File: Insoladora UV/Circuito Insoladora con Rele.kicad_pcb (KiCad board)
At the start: 2 copper layers, 120 x 60 mm, 38 parts, among them J1 Entrada 5V/2A, J2 RELE1, J3 RELE2, K1 SANYOU_SRD_Form_C, K2 SANYOU_SRD_Form_C, Q1 BC548, Q2 BC548, SW1 RESET, SW2 UP, SW3 DOWN, SW4 START/STOP, U1 PIC16F886-IP, U2 PC817, U3 PC817

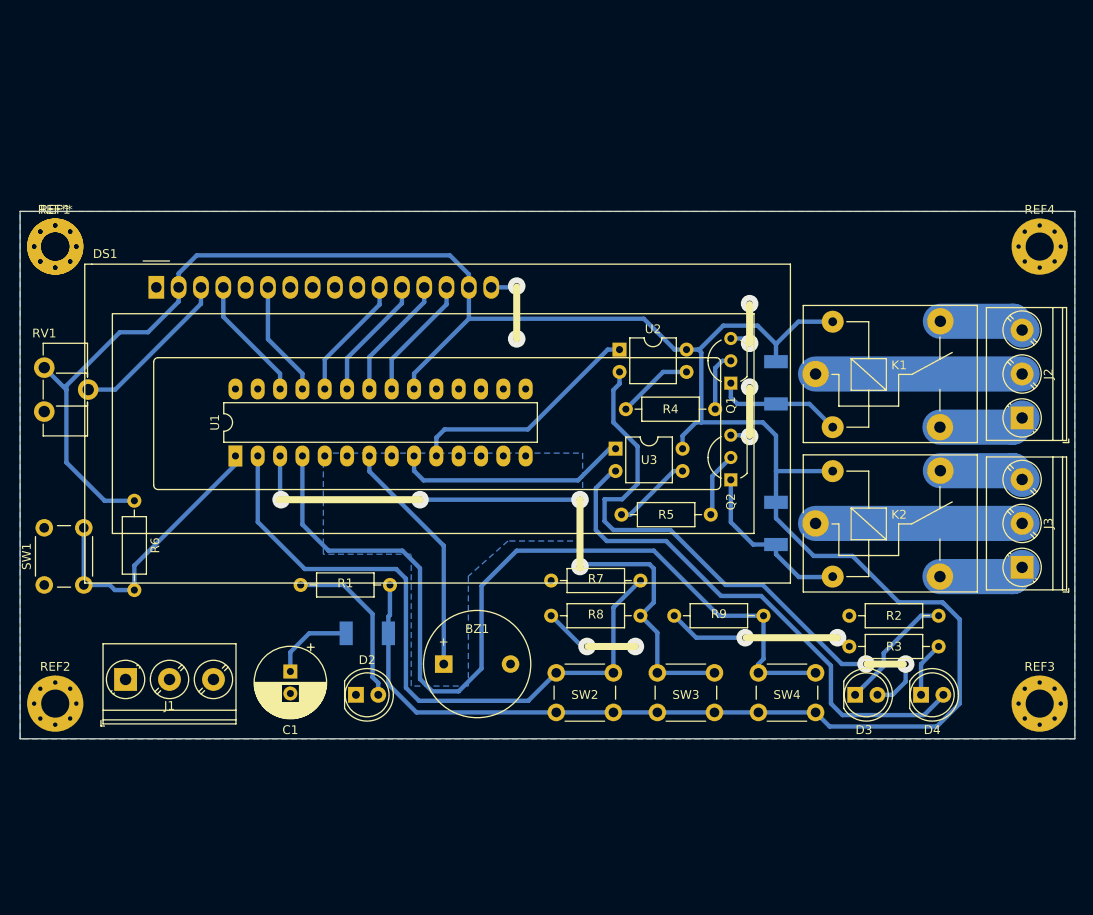
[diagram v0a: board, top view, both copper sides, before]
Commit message: Insoladora
Se termino la pcb de 10x10 para la insoladora
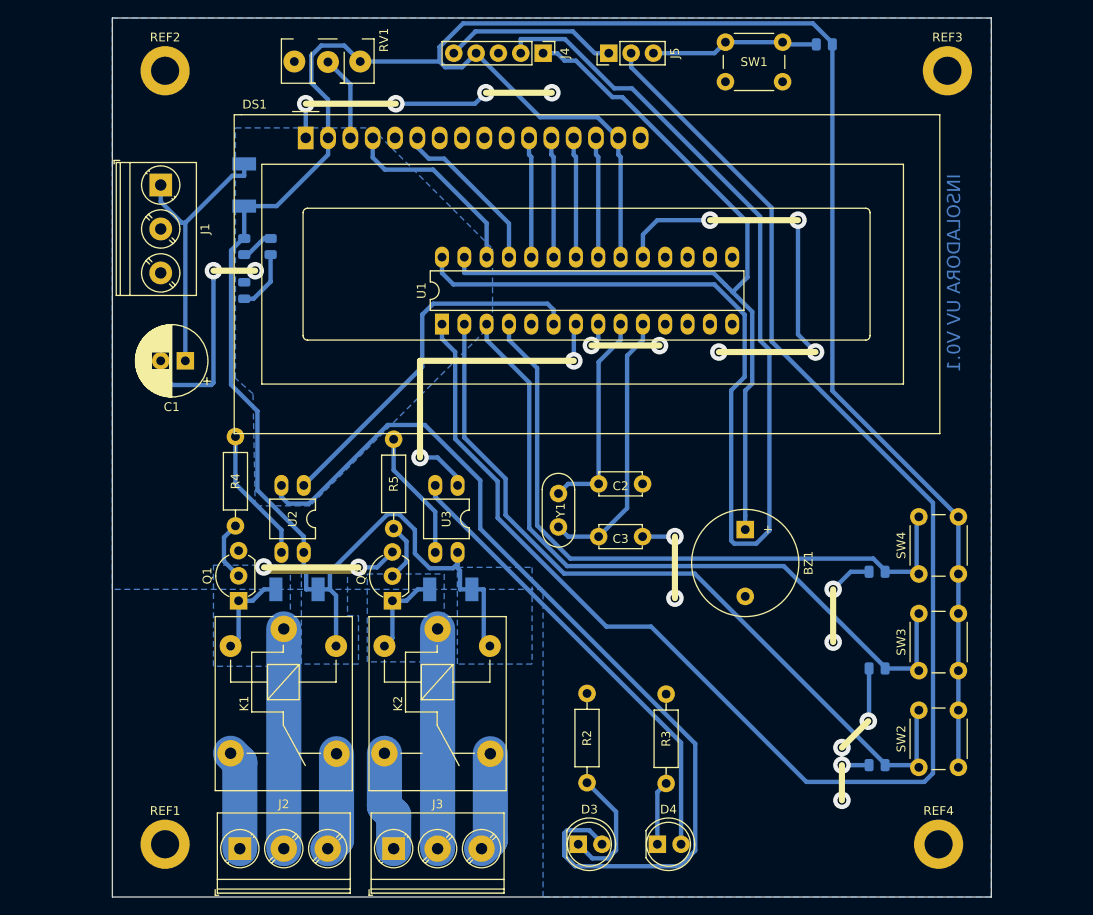
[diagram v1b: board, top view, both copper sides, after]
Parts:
- removed REF**: MountingHole_3.2mm_M3_Pad_Via, MountingHole:MountingHole_3.2mm_M3_Pad_Via
- added C2: C, Capacitor_THT:C_Disc_D4.7mm_W2.5mm_P5.00mm, F.Cu at (114.3, 92.0)
- added C3: C, Capacitor_THT:C_Disc_D4.7mm_W2.5mm_P5.00mm, F.Cu at (114.3, 98.0)
- added J4: Conn_01x05_Male, Connector_PinHeader_2.54mm:PinHeader_1x05_P2.54mm_Vertical, F.Cu at (103.0, 43.0)
- added J5: Conn_01x03_Male, Connector_PinHeader_2.54mm:PinHeader_1x03_P2.54mm_Vertical, F.Cu at (110.5, 43.0)
- added R10: 100/0.125W, Resistor_SMD:R_0805_2012Metric, B.Cu at (72.0, 65.0)
- added Y1: Crystal, Crystal:Crystal_HC52-8mm_Vertical, F.Cu at (104.8, 93.1)
- D2: footprint LED_THT:LED_D5.0mm -> LED_SMD:LED_0805_2012Metric; moved to B.Cu
- R1: value 150/0.25W -> 100/0.125W; footprint Resistor_THT:R_Axial_DIN0207_L6.3mm_D2.5mm_P10.16mm_Horizontal -> Resistor_SMD:R_0805_2012Metric; moved to B.Cu
- R6, R7, R8, R9: footprint Resistor_THT:R_Axial_DIN0207_L6.3mm_D2.5mm_P10.16mm_Horizontal -> Resistor_SMD:R_0805_2012Metric; moved to B.Cu
- REF1, REF2, REF3, REF4: value MountingHole_3.2mm_M3_Pad_Via -> MountingHole_3.2mm_M3_DIN965_Pad; footprint MountingHole:MountingHole_3.2mm_M3_Pad_Via -> MountingHole:MountingHole_3.2mm_M3_DIN965_Pad
- U2, U3: footprint Package_DIP:DIP-4_W7.62mm -> Package_DIP:DIP-4_W7.62mm_LongPads
- moved SW1 101.7 mm to (130.2, 46.2), turned to 180 degrees
- moved J2 101.6 mm to (68.5, 133.5), turned to 0 degrees
- moved R6 94.1 mm to (135.0, 42.0), turned to 180 degrees
- moved J3 78.3 mm to (86.0, 133.5), turned to 0 degrees
- moved REF2 73.1 mm to (60.0, 45.0)
- moved REF3 72.8 mm to (149.0, 45.0)
- moved REF1 69.1 mm to (60.0, 133.0)
- moved REF4 69.0 mm to (148.0, 133.0)
- moved K1 67.1 mm to (73.5, 108.5), turned to -90 degrees
- moved Q1 61.1 mm to (68.4, 105.0)
- moved D5 59.4 mm to (75.0, 104.0), turned to 180 degrees
- moved J1 56.4 mm to (59.5, 58.0), turned to -90 degrees
- moved D1 52.9 mm to (69.0, 58.0), turned to 90 degrees
- moved RV1 51.0 mm to (81.0, 41.5), turned to -90 degrees
- moved D2 47.7 mm to (69.0, 70.0), turned to -90 degrees
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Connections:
- BZ1 pad 1: /BUZZER -> /ICSP_CLK
- DS1 pad 10: GND -> /DB3
- DS1 pad 7: GND -> /DB0
- DS1 pad 8: GND -> /DB1
- DS1 pad 9: GND -> /DB2
- J1 pad 1: Net-(F1-Pad1) -> Net-(C1-Pad1)
- R1 pad 2: Net-(D2-Pad2) -> Net-(R1-Pad2)
- R6 pad 2: /RST -> /RESET
- SW1 pad 2: /RST -> /RESET
- U1 pad 10: /RA6 -> /OSC2
- U1 pad 27: /RB6 -> /ICSP_CLK
- U1 pad 7: /BUZZER -> /RA5
- U1 pad 9: /RA7 -> /OSC1
- U2 pad 1: /RA6 -> /RA4
- U3 pad 1: /RA7 -> /RA5
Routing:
- net /RST: track 32.5 -> 183.2 mm
- net /RB7: track 0.00 -> 143.0 mm
- net GND: track 56.0 -> 170.9 mm, vias 10 -> 22
- net /ICSP_CLK: track 0.00 -> 101.4 mm
- net /RA4: track 0.00 -> 42.4 mm
- net /RA5: track 0.00 -> 38.9 mm, vias 0 -> 2
- net Net-(D3-Pad2): track 68.1 -> 106.7 mm, vias 2 -> 0
- net /OSC2: track 0.00 -> 31.3 mm
- net /RA2: track 103.9 -> 76.4 mm
- net /BUZZER: track 27.2 -> 0.00 mm
- net /RA6: track 27.1 -> 0.00 mm
- net /RA7: track 26.6 -> 0.00 mm
- net /OSC1: track 0.00 -> 24.2 mm
- net Net-(C1-Pad1): track 9.44 -> 31.7 mm
- net /MCLR: track 0.00 -> 19.7 mm
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- added copper zone on B.Cu, net +5V
- added copper zone on B.Cu, net Net-(D5-Pad2)
- added copper zone on B.Cu, net Net-(D6-Pad2)
- removed copper zone on B.Cu, net /BUZZER
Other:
- board size 120 x 60 mm -> 100 x 100 mm
- board text added: "INSOLADORA UV V0.1"
- board text removed: "Insoladora UV V1.0"
- board text removed: "Zuliani Agustin"
